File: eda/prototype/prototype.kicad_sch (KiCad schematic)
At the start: 36 parts, among them J1 Conn_02x05_Odd_Even, U1 8088_Min_Mode, U10 8255A, U11 8253, U12 8259A, U13 8251, U2 GAL16V8, U3 74HC161, U4 74HC574, U5 SST39SF040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

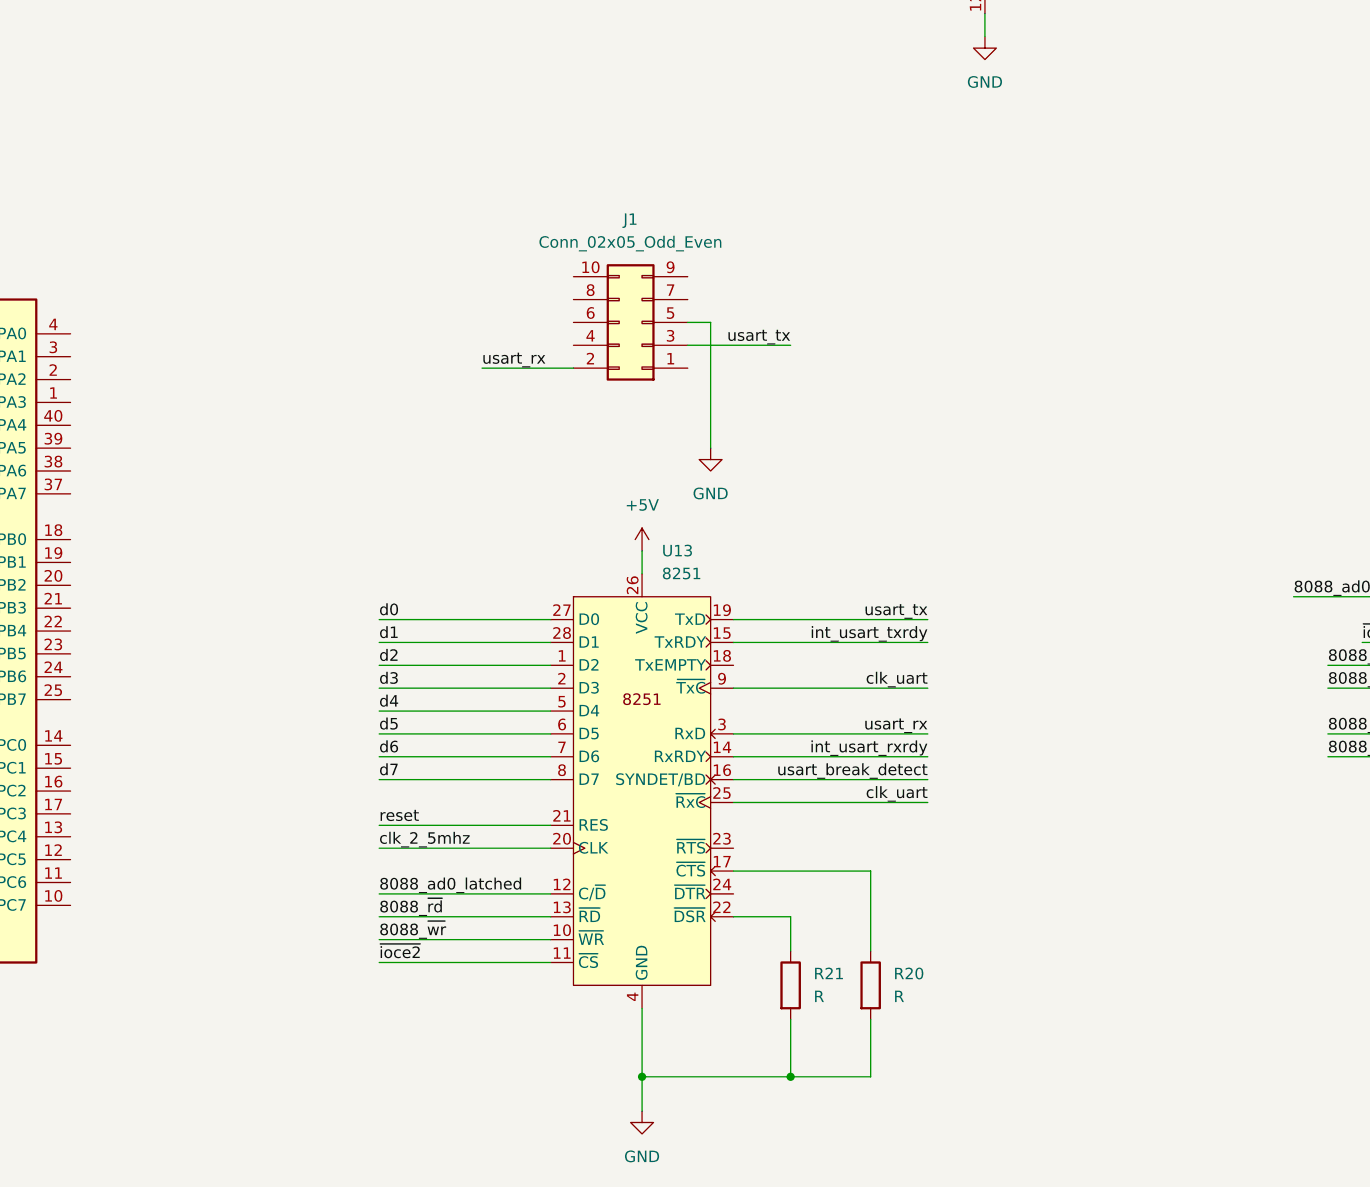
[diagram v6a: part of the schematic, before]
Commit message: eda: prototype: latest changes, uart wiring misc: Try to create a schematic pdf in CI
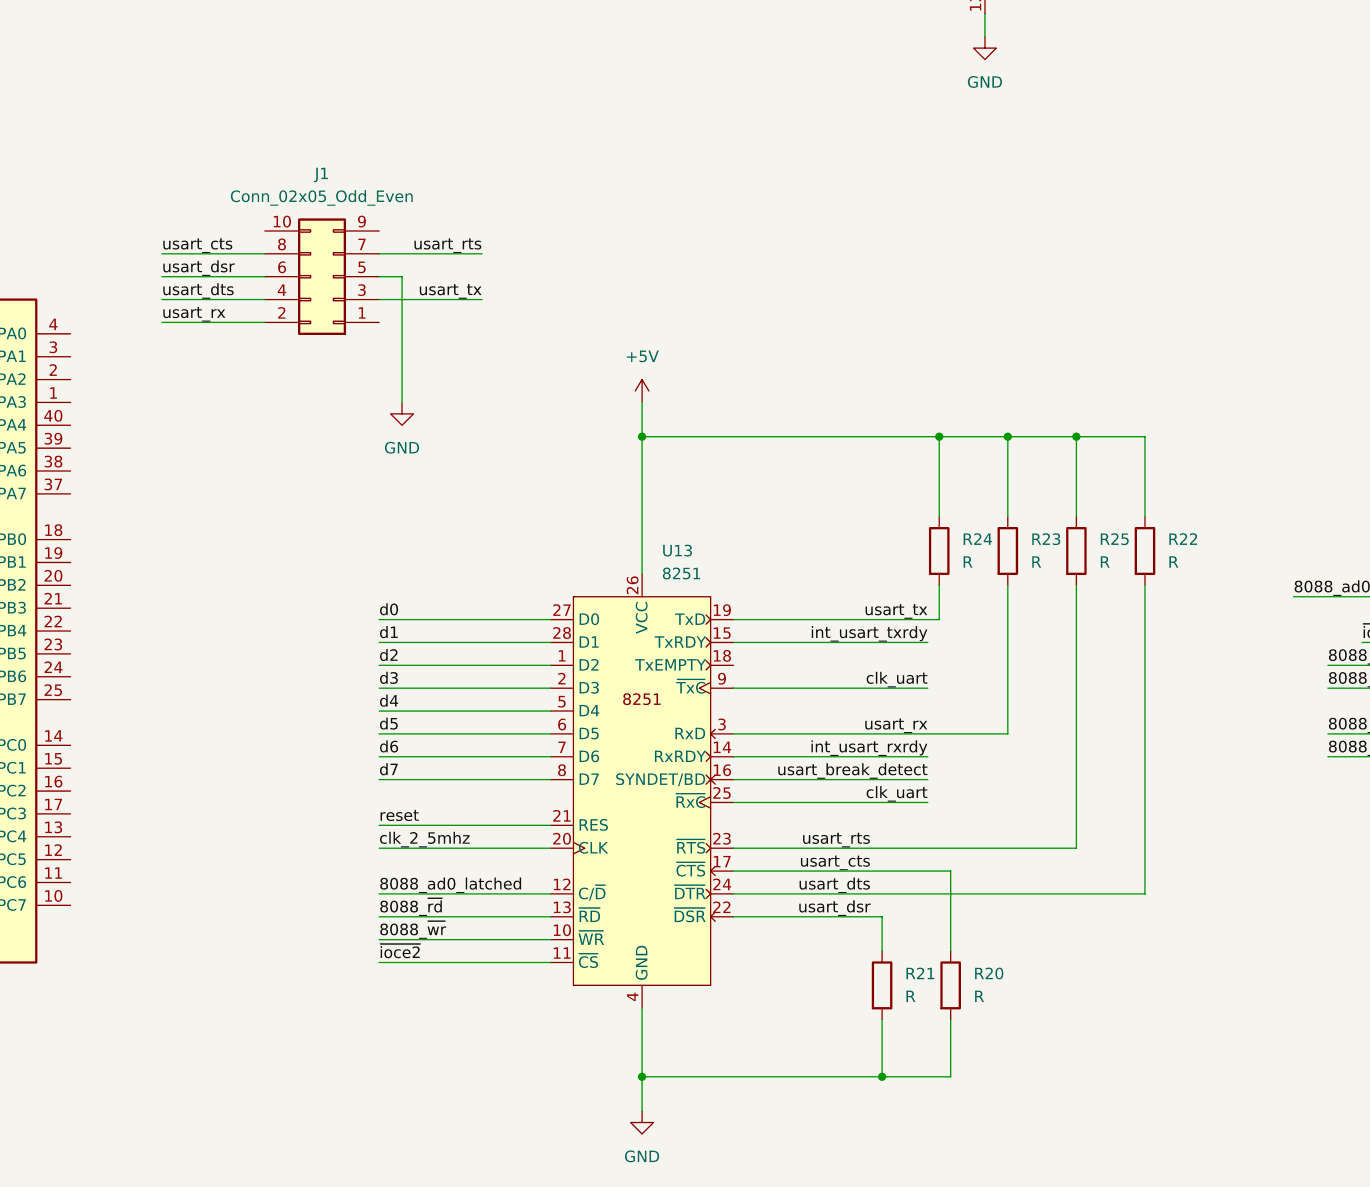
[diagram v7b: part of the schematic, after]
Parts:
- added R22, R23, R24, R25: R, symbol Device:R
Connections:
- net +5V: now also R22.1, R23.1, R24.1, R25.1
- net usart_rx: now also R23.2
- net usart_tx: now also R24.2
- net usart_dts: now reaches J1.4 (Pin_4)
- net usart_dts: now also U13.24 (~{DTR}), R22.2
- net usart_dsr: now reaches J1.6 (Pin_6)
- net usart_dsr: now also R21.1, U13.22 (~{DSR})
- net usart_rts: now reaches J1.7 (Pin_7)
- net usart_rts: now also U13.23 (~{RTS}), R25.2
- net usart_cts: now reaches J1.8 (Pin_8)
- net usart_cts: now also R20.1, U13.17 (~{CTS})
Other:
- moved on the sheet: J1, R20, R21

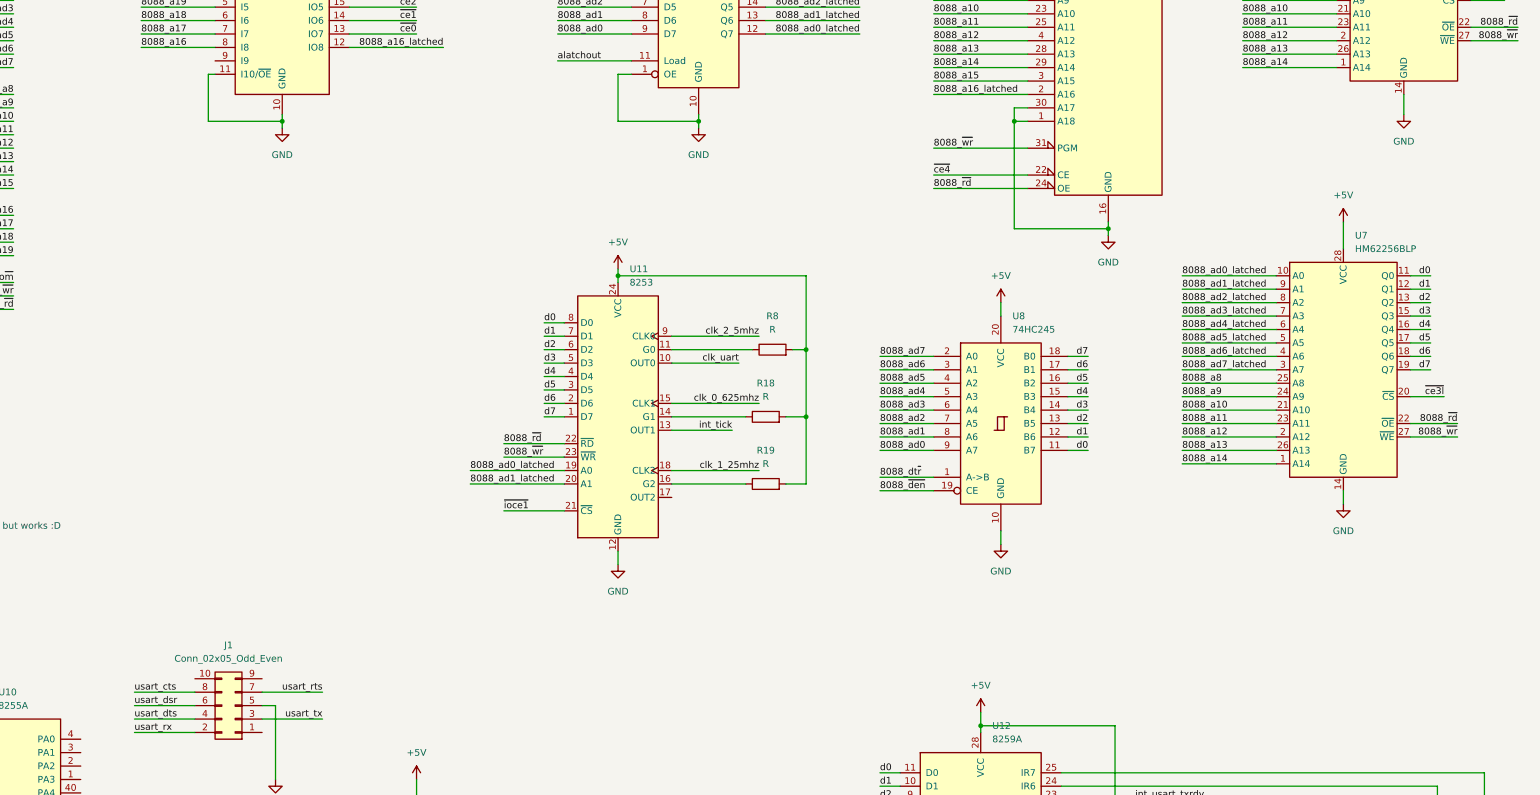
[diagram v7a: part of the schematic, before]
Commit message: eda: prototype: Brain farts for the display level conversion and the dip sw
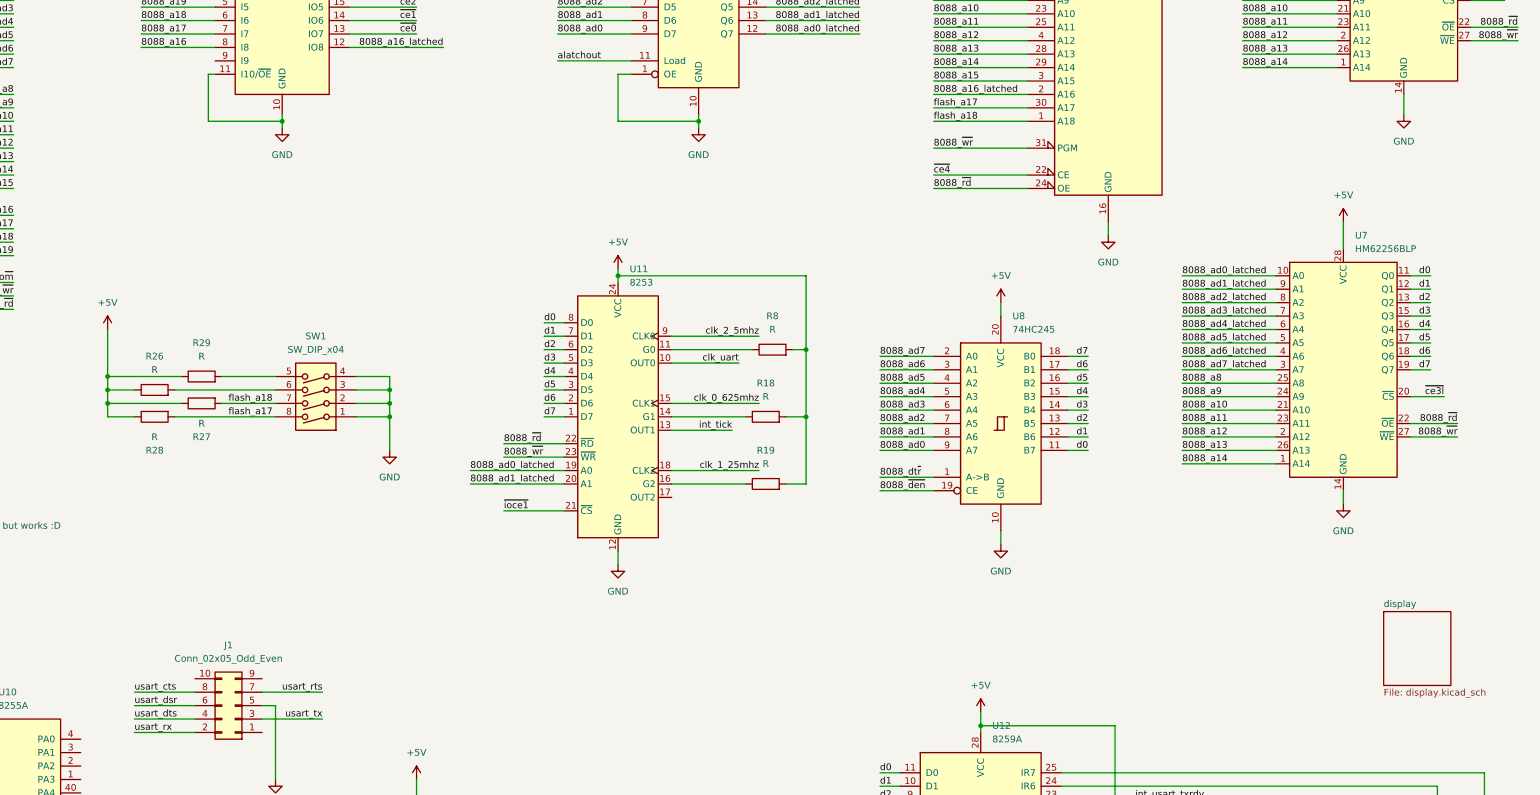
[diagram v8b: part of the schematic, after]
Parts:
- added R26, R27, R28, R29: R, symbol Device:R
- added SW1: SW_DIP_x04, symbol Switch:SW_DIP_x04
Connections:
- net +5V: now also R26.1, R27.1, R28.1, R29.1
- net GND: now also SW1.1, SW1.2, SW1.3, SW1.4; no longer U5.1 (A18), U5.30 (A17)
- new net: R29.2, SW1.5
- new net: R26.2, SW1.6
- new net flash_a17: R28.2, SW1.8, U5.30 (A17)
- new net flash_a18: R27.2, SW1.7, U5.1 (A18)
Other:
- added sheet display (display.kicad_sch)
